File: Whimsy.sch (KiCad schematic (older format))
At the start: 17 parts, among them J1 USB_mini_micro_B, SW1 SW_PUSH, U1 ATMEGA32U4, U1 ProMicro, X1 XTAL_GND

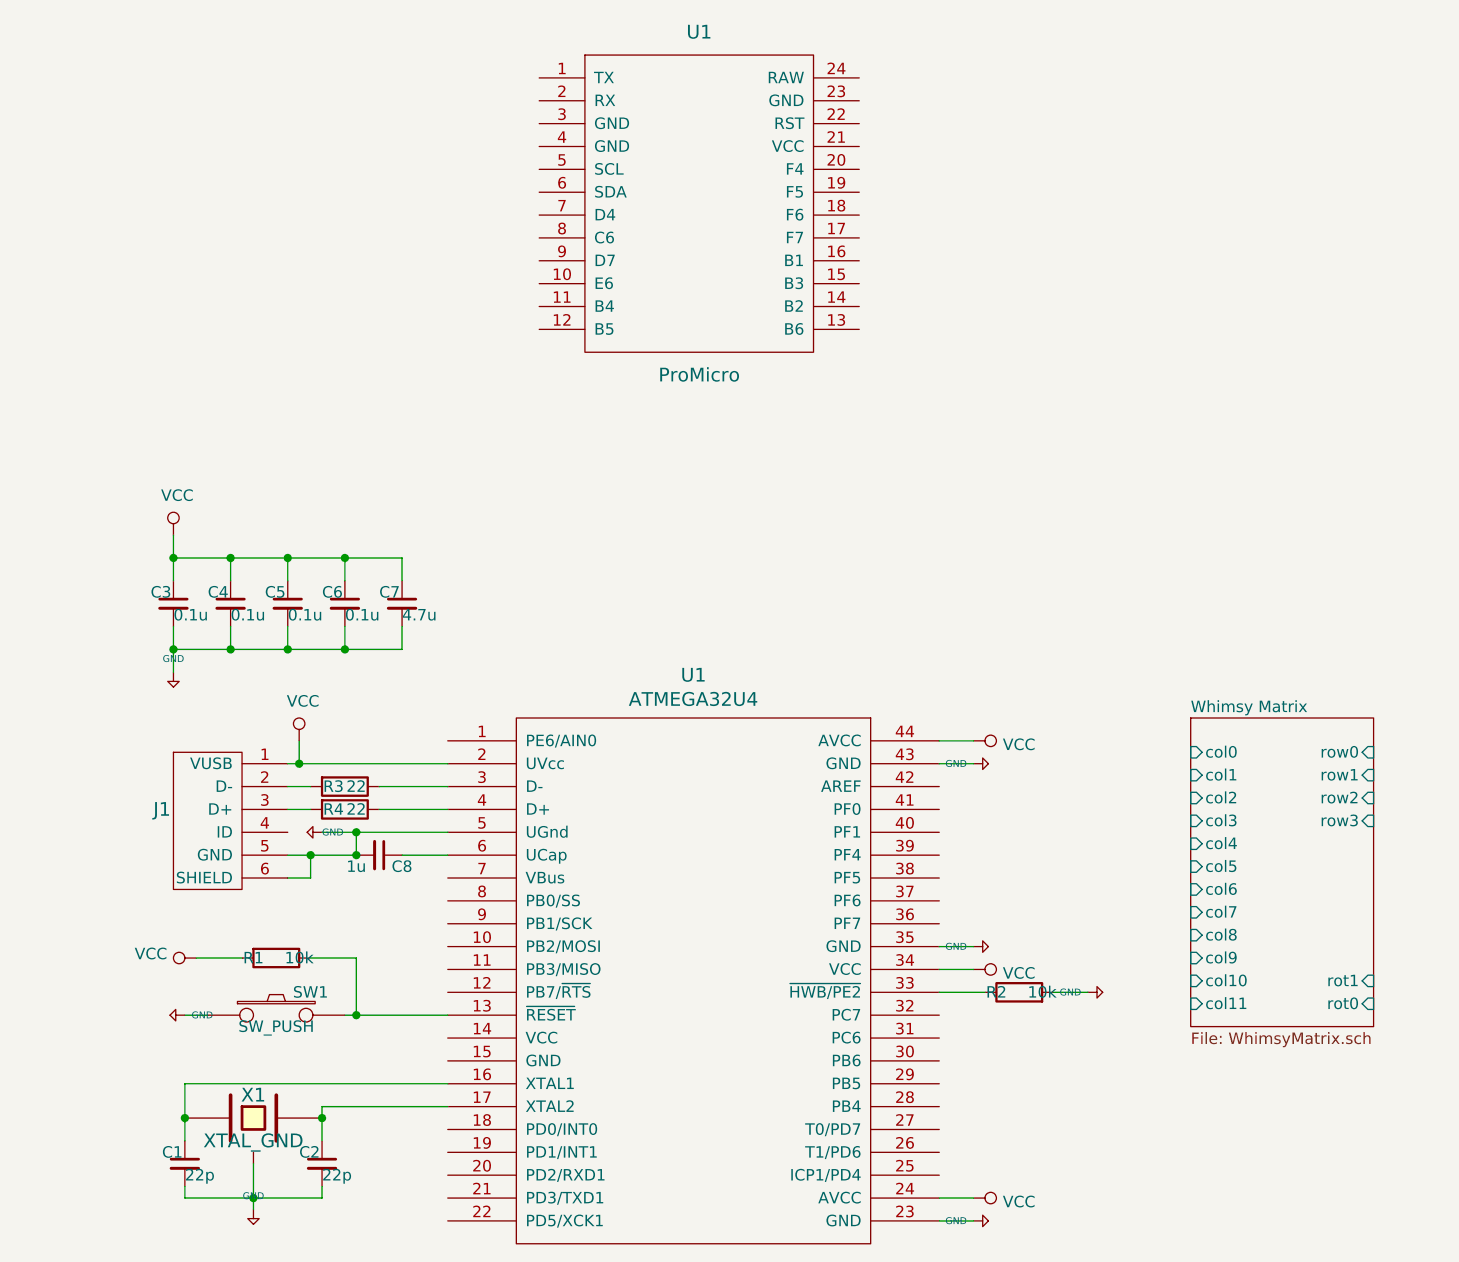
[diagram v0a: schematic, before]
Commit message: added elite-c, changed switch matrix to groups, added LED breakout, added off board reset switch, added OLED pins
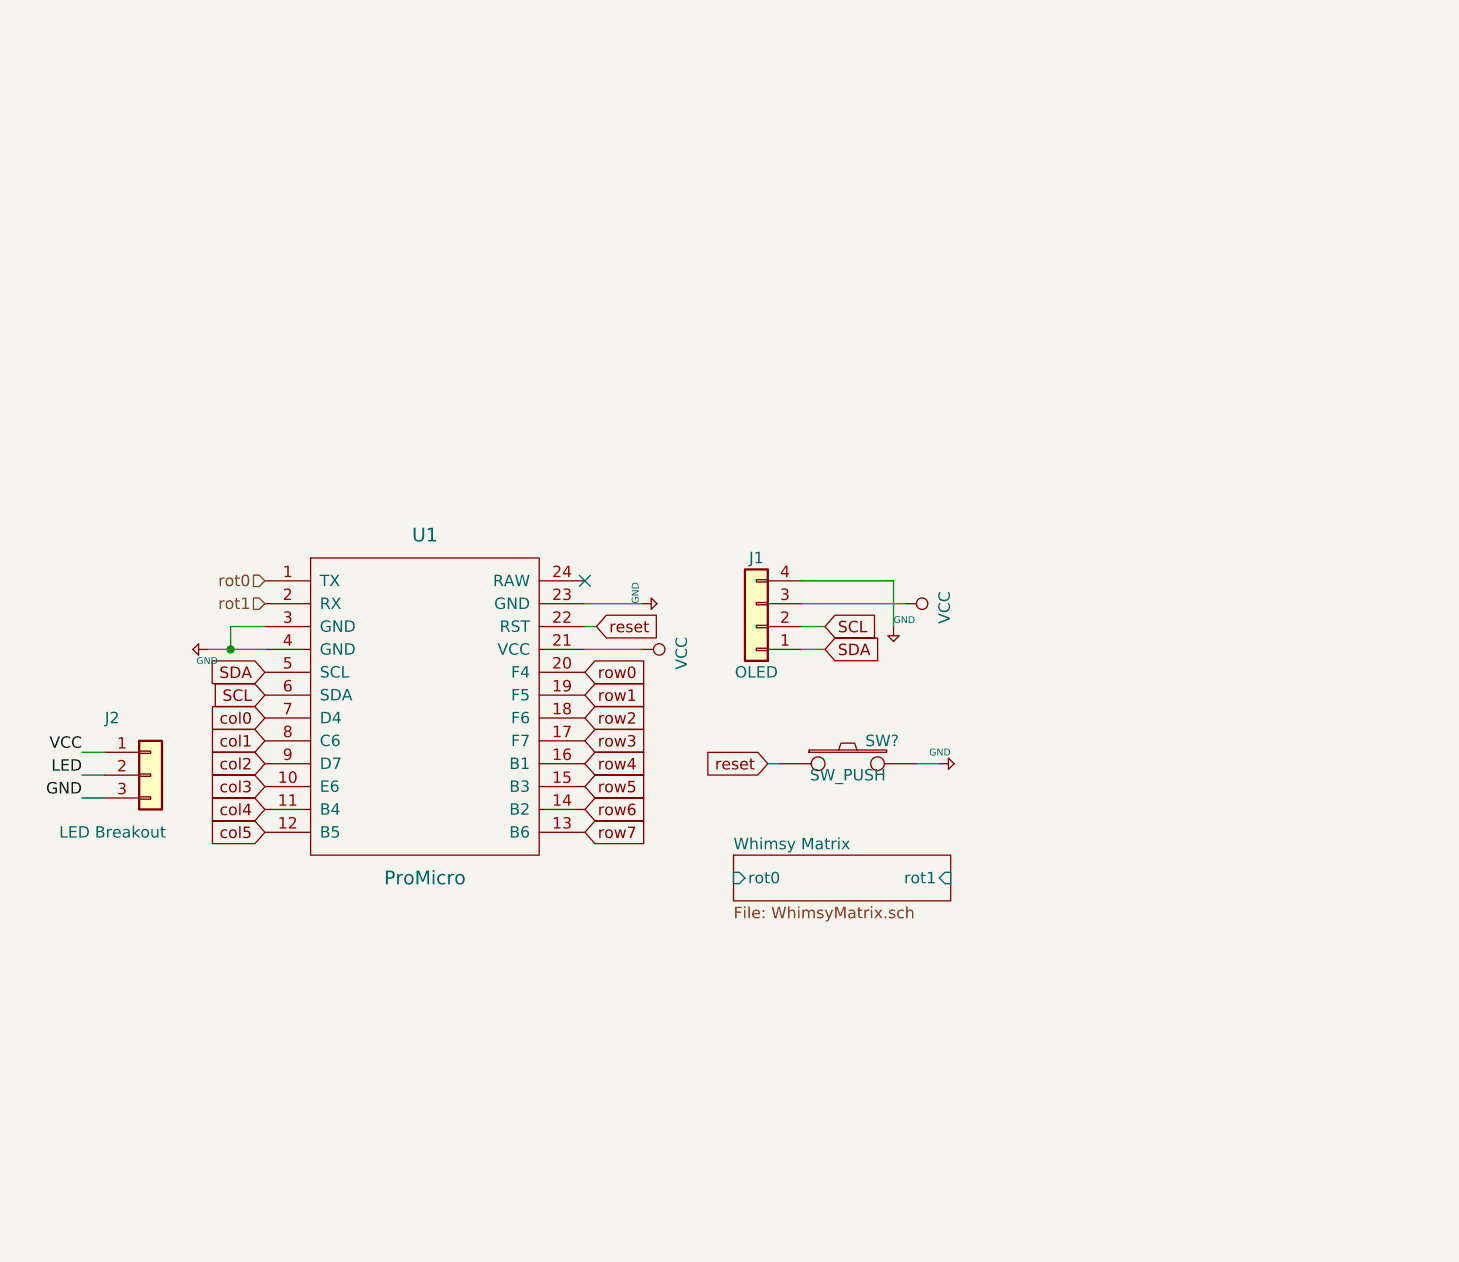
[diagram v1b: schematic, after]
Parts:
- removed C1, C2: 22p, symbol Device:C_Small
- removed C3, C4, C5, C6: 0.1u, symbol Device:C_Small
- removed C7: 4.7u, symbol Device:C_Small
- removed C8: 1u, symbol Device:C_Small
- removed J1: USB_mini_micro_B, symbol keyboard_parts:USB_mini_micro_B
- removed R1, R2: 10k, symbol Device:R
- removed R3, R4: 22, symbol Device:R
- removed SW1: SW_PUSH, symbol keyboard_parts:SW_PUSH
- removed U1: ATMEGA32U4, symbol keyboard_parts:ATMEGA32U4
- removed X1: XTAL_GND, symbol keyboard_parts:XTAL_GND
- added J1: OLED, symbol Connector_Generic:Conn_01x04
- added J2: LED Breakout, symbol Connector_Generic:Conn_01x03
- added SW?: SW_PUSH, symbol keyboard_parts:SW_PUSH
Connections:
- net +5V: now also U1.23 (GND), U1.3 (GND), U1.4 (GND), J1.4 (Pin_4), SW?.2
- net VCC: now also U1.21 (VCC), J1.3 (Pin_3), J2.1 (Pin_1)
- net rot0: now reaches U1.1 (TX)
- net col3: now reaches U1.10 (E6)
- net col4: now reaches U1.11 (B4)
- net col5: now reaches U1.12 (B5)
- net row7: now reaches U1.13 (B6)
- net row6: now reaches U1.14 (B2)
- net row5: now reaches U1.15 (B3)
- net row4: now reaches U1.16 (B1)
- net row3: now reaches U1.17 (F7)
- net row2: now reaches U1.18 (F6)
- net row1: now reaches U1.19 (F5)
- net rot1: now reaches U1.2 (RX)
- net row0: now reaches U1.20 (F4)
- net reset: now reaches U1.22 (RST)
- net reset: now also SW?.1
- net SDA: now reaches U1.5 (SCL)
- net SDA: now also J1.1 (Pin_1)
- net SCL: now reaches U1.6 (SDA)
- net SCL: now also J1.2 (Pin_2)
- net col0: now reaches U1.7 (D4)
- net col1: now reaches U1.8 (C6)
- net col2: now reaches U1.9 (D7)
- new net GND: J2.3 (Pin_3)
- new net LED: J2.2 (Pin_2)
- no-connect marks 0 -> 1
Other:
- moved on the sheet: U1

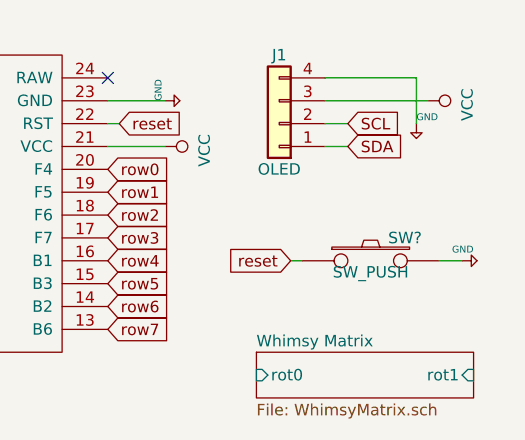
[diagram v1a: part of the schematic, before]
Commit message: duplicate diode (D28) fixed
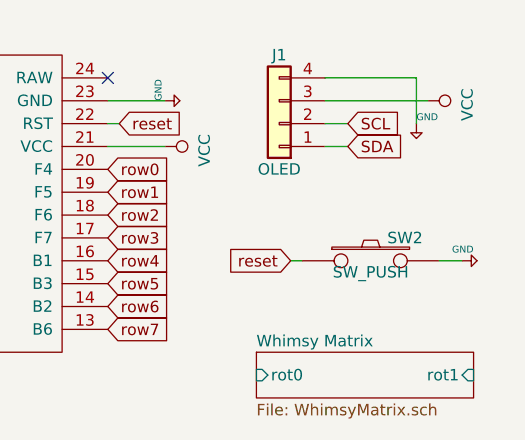
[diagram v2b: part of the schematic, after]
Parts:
- gave numbers to parts that had none: 1
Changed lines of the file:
@@
 F0 "Whimsy Matrix" 50
 F1 "WhimsyMatrix.sch" 50
-F18 "rot1" I R 6650 4700 50
-F19 "rot0" I L 5700 4700 50
+F2 "rot1" I R 6650 4700 50
+F3 "rot0" I L 5700 4700 50
 $EndSheet
 $Bitmap
@@
 $EndBitmap
 $Comp
-L keyboard_parts:SW_PUSH SW?
+L keyboard_parts:SW_PUSH SW2
 U 1 1 5E66E667
 P 6200 4200
-F 0 "SW?" H 6350 4300 50  0000 C CNN
+F 0 "SW2" H 6350 4300 50  0000 C CNN
 F 1 "SW_PUSH" H 6200 4150 50  0000 C CNN
 F 2 "" H 6200 4200 60  0000 C CNN
@@
 $EndComp
 $Comp
-L keyboard_parts:GND #PWR?
+L keyboard_parts:GND #PWR0101
 U 1 1 5E66EAA6
 P 6600 4200
-F 0 "#PWR?" H 6600 4250 20  0001 C CNN
+F 0 "#PWR0101" H 6600 4250 20  0001 C CNN
 F 1 "GND" V 6650 4150 30  0000 L CNN
 F 2 "" H 6600 4200 60  0000 C CNN
@@
 $EndComp
 $Comp
-L keyboard_parts:GND #PWR?
+L keyboard_parts:GND #PWR0102
 U 1 1 5E67912E
 P 6400 3600
-F 0 "#PWR?" H 6400 3650 20  0001 C CNN
+F 0 "#PWR0102" H 6400 3650 20  0001 C CNN
 F 1 "GND" H 6400 3629 30  0000 L CNN
 F 2 "" H 6400 3600 60  0000 C CNN
@@
 $EndComp
 $Comp
-L power:VCC #PWR?
+L power:VCC #PWR0103
 U 1 1 5E679971
 P 6450 3500
-F 0 "#PWR?" H 6450 3350 50  0001 C CNN
+F 0 "#PWR0103" H 6450 3350 50  0001 C CNN
 F 1 "VCC" H 6467 3673 50  0000 C CNN
 F 2 "" H 6450 3500 50  0001 C CNN
@@
 	5850 4200 5900 4200
 $Comp
-L keyboard_parts:GND #PWR?
+L keyboard_parts:GND #PWR0104
 U 1 1 5E6ABEA3
 P 3400 3700
-F 0 "#PWR?" H 3400 3750 20  0001 C CNN
+F 0 "#PWR0104" H 3400 3750 20  0001 C CNN
 F 1 "GND" V 3450 3650 30  0000 L CNN
 F 2 "" H 3400 3700 60  0000 C CNN
@@
 	5050 3600 5100 3600
 $Comp
-L power:VCC #PWR?
+L power:VCC #PWR0105
 U 1 1 5E6AEA7D
 P 5300 3700
-F 0 "#PWR?" H 5300 3550 50  0001 C CNN
+F 0 "#PWR0105" H 5300 3550 50  0001 C CNN
 F 1 "VCC" H 5317 3873 50  0000 C CNN
 F 2 "" H 5300 3700 50  0001 C CNN
@@
 $EndComp
 $Comp
-L keyboard_parts:GND #PWR?
+L keyboard_parts:GND #PWR0106
 U 1 1 5E6AF358
 P 5300 3500
-F 0 "#PWR?" H 5300 3550 20  0001 C CNN
+F 0 "#PWR0106" H 5300 3550 20  0001 C CNN
 F 1 "GND" H 5300 3529 30  0000 L CNN
 F 2 "" H 5300 3500 60  0000 C CNN

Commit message: first layout test
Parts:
- J1: footprint (none) -> SofleKeyboard-footprint:OLED_4Pin
- J2: footprint (none) -> SofleKeyboard-footprint:LED
- SW2: footprint (none) -> SofleKeyboard-footprint:TACT_SWITCH_TVBP06
- U1: footprint (none) -> Keebio-Parts:Elite-C
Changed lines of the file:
@@
 F 0 "SW2" H 6350 4300 50  0000 C CNN
 F 1 "SW_PUSH" H 6200 4150 50  0000 C CNN
-F 2 "" H 6200 4200 60  0000 C CNN
+F 2 "SofleKeyboard-footprint:TACT_SWITCH_TVBP06" H 6200 4200 60  0001 C CNN
 F 3 "" H 6200 4200 60  0000 C CNN
 	1    6200 4200
@@
 F 0 "J1" H 5800 3300 50  0000 C CNN
 F 1 "OLED" H 5800 3800 50  0000 C CNN
-F 2 "" H 5800 3600 50  0001 C CNN
+F 2 "SofleKeyboard-footprint:OLED_4Pin" H 5800 3600 50  0001 C CNN
 F 3 "~" H 5800 3600 50  0001 C CNN
 	1    5800 3600
@@
 F 0 "U1" H 4350 5100 60  0000 C CNN
 F 1 "ProMicro" H 4350 3600 60  0000 C CNN
-F 2 "" H 4450 3100 60  0000 C CNN
+F 2 "Keebio-Parts:Elite-C" H 4450 3100 60  0001 C CNN
 F 3 "" H 4450 3100 60  0000 C CNN
 	1    4350 4150
@@
 F 0 "J2" H 2950 4500 50  0000 L CNN
 F 1 "LED Breakout" H 2750 4000 50  0000 L CNN
-F 2 "" H 3150 4250 50  0001 C CNN
+F 2 "SofleKeyboard-footprint:LED" H 3150 4250 50  0001 C CNN
 F 3 "~" H 3150 4250 50  0001 C CNN
 	1    3150 4250

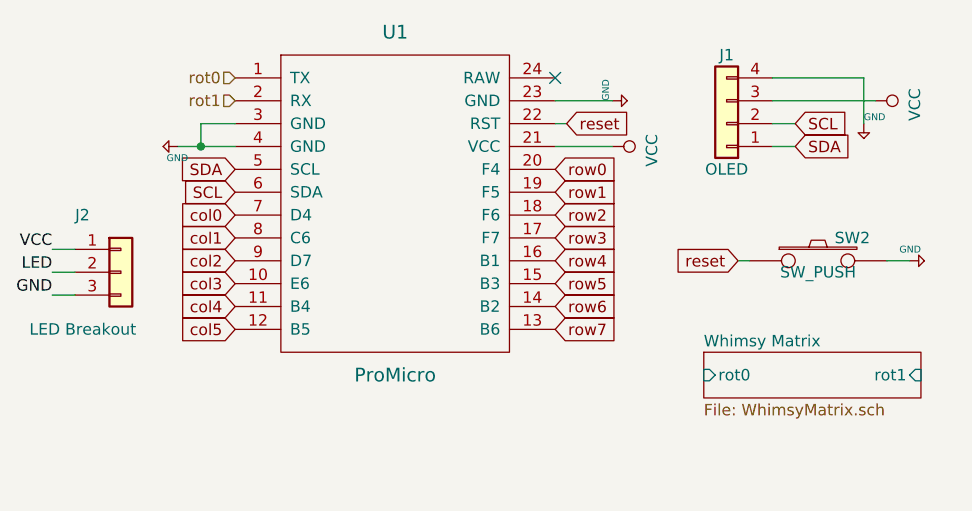
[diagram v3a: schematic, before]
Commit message: better routing, columns, rows and via's to connect to the elite c
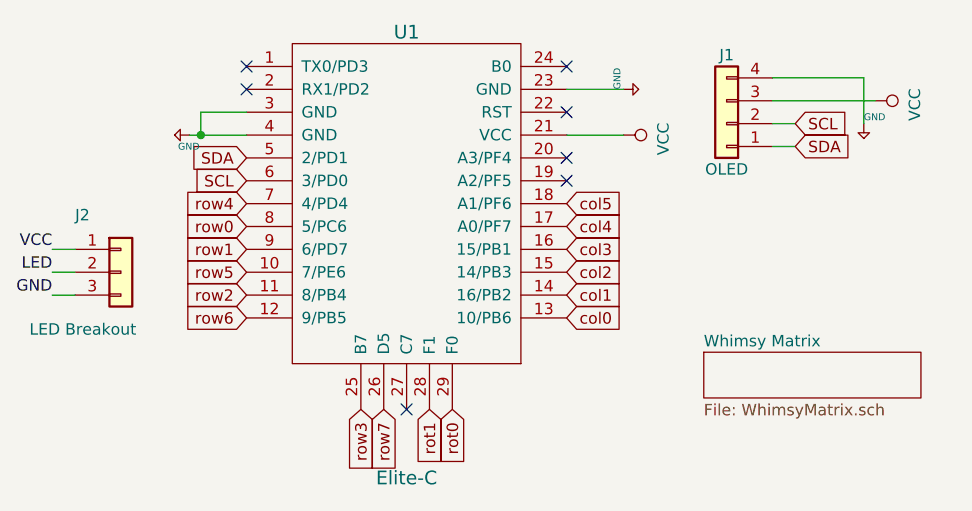
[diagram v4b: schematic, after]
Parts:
- removed SW2: SW_PUSH, SofleKeyboard-footprint:TACT_SWITCH_TVBP06, symbol keyboard_parts:SW_PUSH
- removed U1: ProMicro, Keebio-Parts:Elite-C, symbol promicro:ProMicro
- added U1: Elite-C, Keebio-Parts:Elite-C-NoSilk, symbol minato-cache:keebio-components_Elite-C
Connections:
- net +5V: now also U1.23 (GND), U1.3 (GND), U1.4 (GND)
- net SCL: now also U1.6 (3/PD0)
- net SDA: now also U1.5 (2/PD1)
- net VCC: now also U1.21 (VCC)
- net col0: now also U1.13 (10/PB6)
- net col1: now also U1.14 (16/PB2)
- net col2: now also U1.15 (14/PB3)
- net col3: now also U1.16 (15/PB1)
- net col4: now also U1.17 (A0/PF7)
- net col5: now also U1.18 (A1/PF6)
- net rot0: now also U1.29 (F0)
- net rot1: now also U1.28 (F1)
- net row0: now also U1.8 (5/PC6)
- net row1: now also U1.9 (6/PD7)
- net row2: now also U1.11 (8/PB4)
- net row3: now also U1.25 (B7)
- net row4: now also U1.7 (4/PD4)
- net row5: now also U1.10 (7/PE6)
- net row6: now also U1.12 (9/PB5)
- net row7: now also U1.26 (D5)
- no-connect marks 1 -> 7
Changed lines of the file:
@@
 encoding utf-8
 Sheet 1 2
-Title "Whimsey"
-Date "2020-03-03"
-Rev "A"
+Title "Whimsy"
+Date "2020-03-05"
+Rev "0.1"
 Comp "Prkns"
 Comment1 ""
@@
 F0 "Whimsy Matrix" 50
 F1 "WhimsyMatrix.sch" 50
-F2 "rot1" I R 6650 4700 50
-F3 "rot0" I L 5700 4700 50
 $EndSheet
 $Bitmap
@@
 $EndBitmap
 $Comp
-L keyboard_parts:SW_PUSH SW2
-U 1 1 5E66E667
-P 6200 4200
-F 0 "SW2" H 6350 4300 50  0000 C CNN
-F 1 "SW_PUSH" H 6200 4150 50  0000 C CNN
-F 2 "SofleKeyboard-footprint:TACT_SWITCH_TVBP06" H 6200 4200 60  0001 C CNN
-F 3 "" H 6200 4200 60  0000 C CNN
-	1    6200 4200
-	1    0    0    -1
-$EndComp
-$Comp
-L keyboard_parts:GND #PWR0101
-U 1 1 5E66EAA6
-P 6600 4200
-F 0 "#PWR0101" H 6600 4250 20  0001 C CNN
-F 1 "GND" V 6650 4150 30  0000 L CNN
-F 2 "" H 6600 4200 60  0000 C CNN
-F 3 "" H 6600 4200 60  0000 C CNN
-	1    6600 4200
-	0    -1   -1   0
-$EndComp
-$Comp
 L keyboard_parts:GND #PWR0102
 U 1 1 5E67912E
@@
 Wire Wire Line
 	6000 3600 6100 3600
-Wire Wire Line
-	6500 4200 6600 4200
-Wire Wire Line
-	5850 4200 5900 4200
 $Comp
 L keyboard_parts:GND #PWR0104
 U 1 1 5E6ABEA3
-P 3400 3700
-F 0 "#PWR0104" H 3400 3750 20  0001 C CNN
-F 1 "GND" V 3450 3650 30  0000 L CNN
-F 2 "" H 3400 3700 60  0000 C CNN
-F 3 "" H 3400 3700 60  0000 C CNN
-	1    3400 3700
+P 3450 3650
+F 0 "#PWR0104" H 3450 3700 20  0001 C CNN
+F 1 "GND" V 3500 3600 30  0000 L CNN
+F 2 "" H 3450 3650 60  0000 C CNN
+F 3 "" H 3450 3650 60  0000 C CNN
+	1    3450 3650
 	0    1    1    0
 $EndComp
-Wire Wire Line
-	3500 3600 3650 3600
-Wire Wire Line
-	3650 3700 3500 3700
-Wire Wire Line
-	3500 3600 3500 3700
-Wire Wire Line
-	3400 3700 3500 3700
-Connection ~ 3500 3700
-Wire Wire Line
-	5050 3600 5100 3600
 $Comp
 L power:VCC #PWR0105
 U 1 1 5E6AEA7D
-P 5300 3700
-F 0 "#PWR0105" H 5300 3550 50  0001 C CNN
-F 1 "VCC" H 5317 3873 50  0000 C CNN
-F 2 "" H 5300 3700 50  0001 C CNN
-F 3 "" H 5300 3700 50  0001 C CNN
-	1    5300 3700
+P 5350 3650
+F 0 "#PWR0105" H 5350 3500 50  0001 C CNN
+F 1 "VCC" H 5367 3823 50  0000 C CNN
+F 2 "" H 5350 3650 50  0001 C CNN
+F 3 "" H 5350 3650 50  0001 C CNN
+	1    5350 3650
 	0    1    1    0
 $EndComp
@@
 L keyboard_parts:GND #PWR0106
 U 1 1 5E6AF358
-P 5300 3500
-F 0 "#PWR0106" H 5300 3550 20  0001 C CNN
-F 1 "GND" H 5300 3529 30  0000 L CNN
-F 2 "" H 5300 3500 60  0000 C CNN
-F 3 "" H 5300 3500 60  0000 C CNN
-	1    5300 3500
+P 5350 3450
+F 0 "#PWR0106" H 5350 3500 20  0001 C CNN
+F 1 "GND" H 5350 3479 30  0000 L CNN
+F 2 "" H 5350 3450 60  0000 C CNN
+F 3 "" H 5350 3450 60  0000 C CNN
+	1    5350 3450
 	0    -1   -1   0
 $EndComp
-Wire Wire Line
-	5050 3500 5300 3500
-Wire Wire Line
-	5050 3700 5300 3700
-NoConn ~ 5050 3400
 Text GLabel 6100 3700 2    50   Input ~ 0
 SDA
@@
 	-1   0    0    1
 $EndComp
-Text GLabel 5850 4200 0    50   Input ~ 0
-reset
-Text GLabel 5100 3600 2    50   Input ~ 0
-reset
-Text GLabel 3650 3800 0    50   Input ~ 0
+Text GLabel 3700 3750 0    50   Input ~ 0
 SDA
-Text GLabel 3650 3900 0    50   Input ~ 0
+Text GLabel 3700 3850 0    50   Input ~ 0
 SCL
-Text GLabel 3650 4000 0    50   Input ~ 0
+Text GLabel 5100 4450 2    50   Input ~ 0
 col0
-Text GLabel 3650 4100 0    50   Input ~ 0
+Text GLabel 5100 4350 2    50   Input ~ 0
 col1
-$Comp
-L promicro:ProMicro U1
-U 1 1 5E5EA037
-P 4350 4150
-F 0 "U1" H 4350 5100 60  0000 C CNN
-F 1 "ProMicro" H 4350 3600 60  0000 C CNN
-F 2 "Keebio-Parts:Elite-C" H 4450 3100 60  0001 C CNN
-F 3 "" H 4450 3100 60  0000 C CNN
-	1    4350 4150
-	1    0    0    -1
-$EndComp
-Text GLabel 3650 4200 0    50   Input ~ 0
+Text GLabel 5100 4250 2    50   Input ~ 0
 col2
-Text GLabel 3650 4300 0    50   Input ~ 0
+Text GLabel 5100 4150 2    50   Input ~ 0
 col3
-Text GLabel 5050 3800 2    50   Input ~ 0
+Text GLabel 3700 4050 0    50   Input ~ 0
 row0
-Text GLabel 5050 3900 2    50   Input ~ 0
+Text GLabel 3700 4150 0    50   Input ~ 0
 row1
-Text GLabel 5050 4000 2    50   Input ~ 0
+Text GLabel 3700 4350 0    50   Input ~ 0
 row2
-Text GLabel 5050 4100 2    50   Input ~ 0
+Text GLabel 4200 4850 3    50   Input ~ 0
 row3
-Text GLabel 5050 4200 2    50   Input ~ 0
+Text GLabel 3700 3950 0    50   Input ~ 0
 row4
-Text GLabel 5050 4300 2    50   Input ~ 0
+Text GLabel 3700 4250 0    50   Input ~ 0
 row5
-Text GLabel 5050 4400 2    50   Input ~ 0
+Text GLabel 3700 4450 0    50   Input ~ 0
 row6
-Text GLabel 5050 4500 2    50   Input ~ 0
+Text GLabel 4300 4850 3    50   Input ~ 0
 row7
-Text GLabel 3650 4400 0    50   Input ~ 0
+Text GLabel 5100 4050 2    50   Input ~ 0
 col4
-Text GLabel 3650 4500 0    50   Input ~ 0
+Text GLabel 5100 3950 2    50   Input ~ 0
 col5
 $Comp
@@
 Wire Wire Line
 	2950 4350 2850 4350
-Text HLabel 3650 3400 0    50   Input ~ 0
+Text GLabel 4600 4850 3    50   Input ~ 0
 rot0
-Text HLabel 3650 3500 0    50   Input ~ 0
+Text GLabel 4500 4850 3    50   Input ~ 0
 rot1
+$Comp
+L minato-cache:keebio-components_Elite-C U1
+U 1 1 5E7BE733
+P 4400 3900
+F 0 "U1" H 4400 4600 60  0000 C CNN
+F 1 "Elite-C" H 4400 2650 60  0000 C CNN
+F 2 "Keebio-Parts:Elite-C-NoSilk" V 5450 1400 60  0001 C CNN
+F 3 "" V 5450 1400 60  0001 C CNN
+	1    4400 3900
+	1    0    0    -1
+$EndComp
+Wire Wire Line
+	3700 3650 3500 3650
+Wire Wire Line
+	3700 3550 3500 3550
+Wire Wire Line
+	3500 3550 3500 3650
+Connection ~ 3500 3650
+Wire Wire Line
+	3500 3650 3450 3650
+Wire Wire Line
+	5100 3450 5350 3450
+Wire Wire Line
+	5100 3650 5350 3650
+NoConn ~ 5100 3850
+NoConn ~ 5100 3750
+NoConn ~ 5100 3350
+NoConn ~ 3700 3450
+NoConn ~ 3700 3350
+NoConn ~ 4400 4850
+NoConn ~ 5100 3550
 $EndSCHEMATC
